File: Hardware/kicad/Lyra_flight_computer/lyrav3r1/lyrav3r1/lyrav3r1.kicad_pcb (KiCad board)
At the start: 4 copper layers, 25 x 55 mm, 89 parts, among them IC1 TESEO-LIV3F, J1 Conn_01x02, J2 Screw_Terminal_01x02, J4 Conn_01x02, J5 Conn_01x05, J7 USB_B_Micro, J8 Screw_Terminal_01x07, Q1 AO3401A, Q10 AO3400A, Q11 Q_NPN_BEC, Q2 AO3400A, Q3 AO3400A, Q4 AO3400A, Q5 AO3400A, Q7 AO3400A, Q8 AO3400A, Q9 AO3400A, U1 E22-400MM22S, U10 MT2492, U2 BMI088, U3 BMP388, U5 ADXL375BCCZ-RL7, U7 WS7916S-6/TR, U8 RP2040, U9 W25Q128JVS, X2 SX1M12.000M10F30TNN

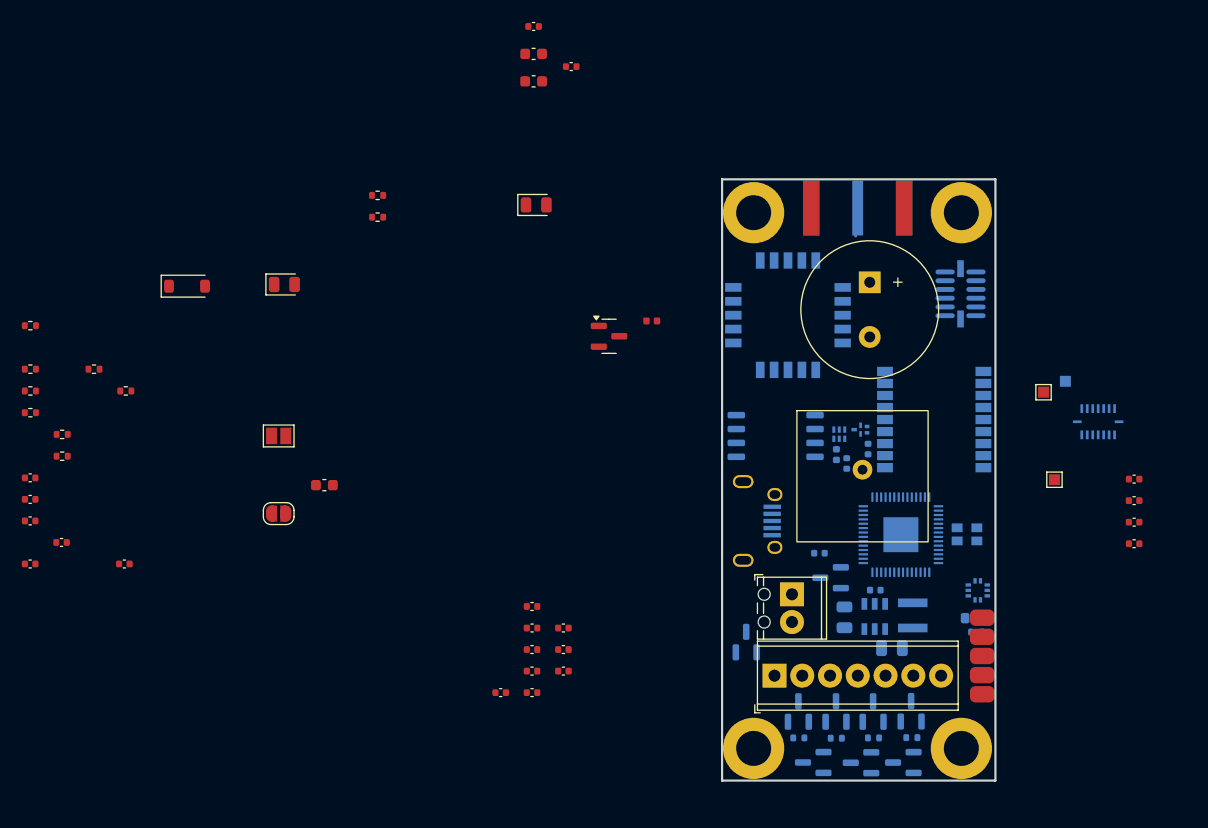
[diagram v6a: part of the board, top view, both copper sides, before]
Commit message: first pass at routing
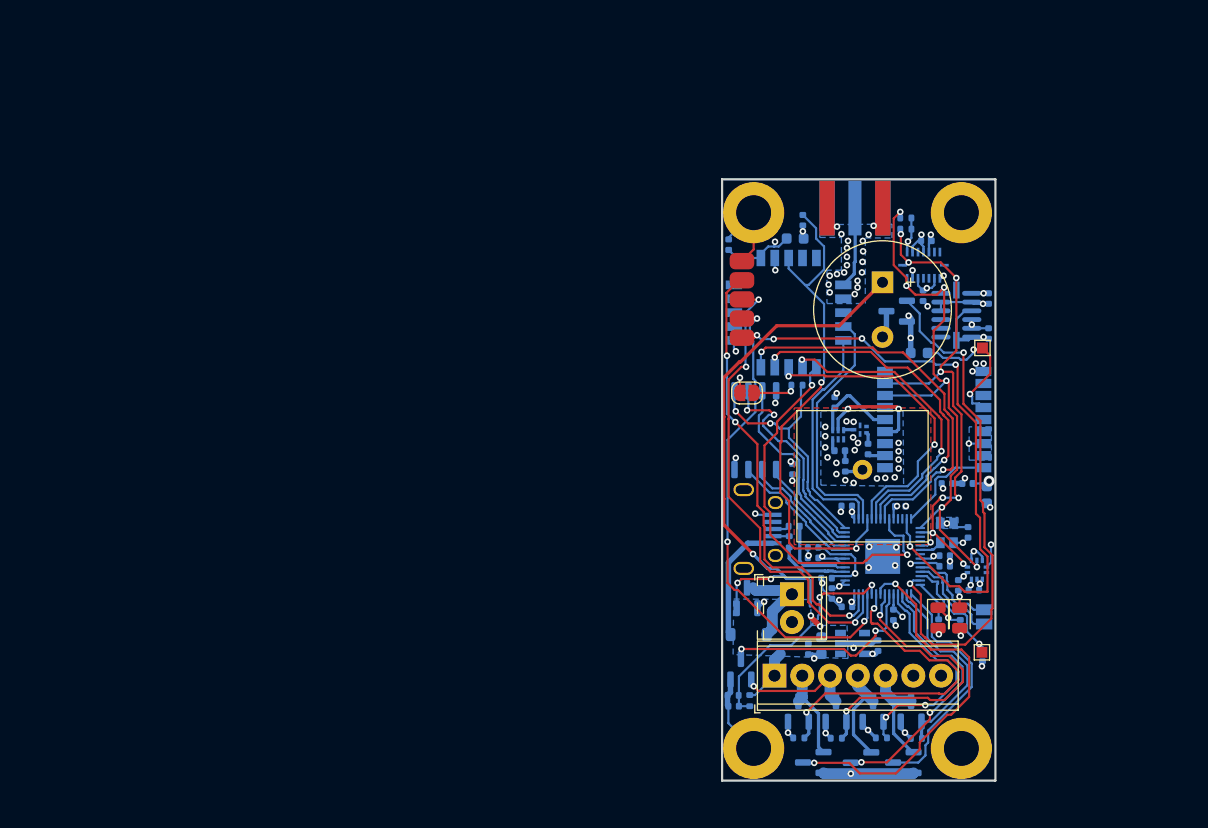
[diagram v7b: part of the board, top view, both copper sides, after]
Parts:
- removed AE2: Antenna, .pretty:SMA-SMD_HJ-SMA086
- removed C8: 1u, Capacitor_SMD:C_0402_1005Metric
- removed C9: 22u, Capacitor_SMD:C_0805_2012Metric
- removed L2: 4.7u, Inductor_SMD:L_Changjiang_FNR3015S
- removed R5: 25k, Resistor_SMD:R_0402_1005Metric
- removed R7: 110k, Resistor_SMD:R_0603_1608Metric
- removed R8: 20k, Resistor_SMD:R_0402_1005Metric
- removed TP3: TestPoint, TestPoint:TestPoint_Pad_1.0x1.0mm
- removed U10: MT2492, .pretty:SOT-23-6_L2.9-W1.6-P0.95-LS2.8-BL
- added AE3: Antenna_Shield, .pretty:CONN-SMD_KH-SMA-KE8-G, B.Cu at (195.8, 66.7)
- added C10: 10n, Capacitor_SMD:C_0402_1005Metric, B.Cu at (184.2, 70.0)
- added C11: 10u, Capacitor_SMD:C_0603_1608Metric, B.Cu at (190.3, 69.4)
- added C29: 100n, Capacitor_SMD:C_0402_1005Metric, B.Cu at (191.0, 67.8)
- added R2: 20k, Resistor_SMD:R_0402_1005Metric, B.Cu at (184.6, 111.2)
- added U6: RT9013-33GB_C19268157, .pretty:SOT-23-5_L2.9-W1.6-P0.95-LS2.8-BR, B.Cu at (195.5, 106.5)
- C1, C12, C13, C14, C16, C17, C18, C19, C2, C20, C21, C22, C24, C25, C26, C27, C28, C3, C32, C34, C4, C50, C7, D1, J1, L1, Q11, R1, R13, R14, R15, R16, R18, R28, R3, R4: moved to B.Cu
- C5: value 22u -> 1u; footprint Capacitor_SMD:C_0805_2012Metric -> Capacitor_SMD:C_0402_1005Metric
- C6: value 22nf -> 1u
- U1: value E22-400MM22S -> E22-900MM22S
- moved R1 92.2 mm to (207.4, 107.6), turned to 90 degrees
- moved R3 88.2 mm to (205.4, 104.8), turned to 90 degrees
- moved C2 85.3 mm to (202.3, 69.6), turned to 180 degrees
- moved C1 83.3 mm to (202.0, 74.7), turned to -90 degrees
- moved C13 82.9 mm to (206.1, 96.3), turned to -90 degrees
- moved R28 77.4 mm to (203.4, 104.8), turned to -90 degrees
- moved R4 71.6 mm to (186.1, 111.7), turned to -90 degrees
- moved D2 68.9 mm to (205.3, 104.1), turned to -90 degrees
- moved R14 67.4 mm to (190.4, 82.9), turned to 180 degrees
- moved R15 67.3 mm to (190.2, 95.8)
- moved J1 66.6 mm to (207.6, 104.0), turned to -90 degrees
- moved C3 66.5 mm to (184.7, 112.2), turned to 180 degrees
- moved R18 65.5 mm to (189.7, 97.2), turned to 90 degrees
- moved C27 61.7 mm to (190.0, 90.5), turned to 90 degrees
- moved D1 60.4 mm to (186.0, 105.7), turned to 180 degrees
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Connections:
- C5 pad 1: +BATT -> +3V3
- C6 pad 1: Net-(U10-BS) -> +BATT
- C6 pad 2: Net-(U10-SW) -> GND
- U1 pad 10: unconnected-(U1-RXEN-Pad10) -> /RXEN
- U1 pad 9: unconnected-(U1-TXEN-Pad9) -> /TXEN
- U8 pad 11: /DIO1 -> unconnected-(U8-GPIO8-Pad11)
- U8 pad 13: unconnected-(U8-GPIO10-Pad13) -> /BRKOUT1
- U8 pad 17: /LEDINDICATION -> unconnected-(U8-GPIO14-Pad17)
- U8 pad 18: /BRKOUT1 -> unconnected-(U8-GPIO15-Pad18)
- U8 pad 2: unconnected-(U8-GPIO0-Pad2) -> /RXEN
- U8 pad 27: unconnected-(U8-GPIO16-Pad27) -> /BUZZER
- U8 pad 28: /BUZZER -> /LEDINDICATION
- U8 pad 29: /P1 EN  -> /P1 CONT 
- U8 pad 3: /DIO3 -> /TXEN
- U8 pad 30: /P1 CONT  -> /P1 EN 
- U8 pad 31: /P2 EN  -> /P2 CONT 
- U8 pad 32: /P2 CONT  -> /P2 EN 
- U8 pad 34: /P3 EN  -> /P3 CONT 
- U8 pad 35: /P3 CONT  -> /P3 EN 
- U8 pad 36: /P4 EN  -> /P4 CONT 
- U8 pad 37: /P4 CONT  -> /P4 EN 
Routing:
- net GND: track 0.00 -> 78.2 mm, vias 0 -> 85
- net +BATT: track 0.00 -> 57.6 mm, vias 0 -> 5
- net /BRKOUT1: track 0.00 -> 54.2 mm, vias 0 -> 5
- net /SDA: track 0.00 -> 52.3 mm, vias 0 -> 6
- net +3V3: track 0.00 -> 52.0 mm, vias 0 -> 23
- net /SCL: track 0.00 -> 48.8 mm, vias 0 -> 8
- net /BUZZER: track 0.00 -> 47.5 mm, vias 0 -> 2
- net /SX RST: track 0.00 -> 47.0 mm, vias 0 -> 2
- net /BRKOUT2: track 0.00 -> 43.6 mm, vias 0 -> 3
- net /BRKOUT3: track 0.00 -> 43.2 mm, vias 0 -> 3
- net /BRKOUT4: track 0.00 -> 41.4 mm, vias 0 -> 3
- net /SCK: track 0.00 -> 36.2 mm, vias 0 -> 2
- net /BUSY: track 0.00 -> 36.0 mm, vias 0 -> 2
- net /P4 CONT : track 0.00 -> 34.7 mm, vias 0 -> 2
- net /SX CS: track 0.00 -> 33.0 mm, vias 0 -> 2
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- added copper zone on B.Cu, net +3V3
- added copper zone on B.Cu, net +BATT
- added copper zone on In1.Cu, net /BATT RAW
- added copper zone on B.Cu, net /GPS 3v3
- added copper zone on In1.Cu, net /GPS 3v3
- added copper zone on B.Cu, net GND
- added copper zone on F.Cu, net GND

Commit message: sade
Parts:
- added C8: 100n, Capacitor_SMD:C_0402_1005Metric, B.Cu at (206.7, 73.3)
- added C9: 100n, Capacitor_SMD:C_0402_1005Metric, B.Cu at (205.0, 71.0)
- added G***: LOGO, LOGO, F.Cu at (200.8, 79.5)
- added G***: LOGO, LOGO, F.Cu at (203.0, 91.2)
- added G***: LOGO, LOGO, B.Cu at (189.6, 76.1)
- added U4: LIS3MDLTR, .pretty:LGA-12_L2.0-W2.0-P0.50-BL, B.Cu at (206.9, 71.5)
- moved R4 1.59 mm to (184.6, 111.3), turned to 180 degrees
- moved R2 1.54 mm to (186.1, 111.8), turned to -90 degrees
- moved H1 0.13 mm to (186.6, 67.0)
- moved H2 0.13 mm to (205.6, 67.0)
- moved H3 0.13 mm to (186.6, 116.0)
- moved H4 0.13 mm to (205.6, 116.0)
- moved C18 0.08 mm to (193.2, 100.6)
- moved C19 0.07 mm to (193.6, 102.0)
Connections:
- R2 pad 1: /BATT SENSE  -> +BATT
- R2 pad 2: GND -> /BATT SENSE 
- R4 pad 1: +BATT -> /BATT SENSE 
- R4 pad 2: /BATT SENSE  -> GND
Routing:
- net GND: track 78.2 -> 95.9 mm, vias 85 -> 88
- net /SDA: track 52.3 -> 63.2 mm, vias 6 -> 7
- net /SCL: track 48.8 -> 53.8 mm, vias 8 -> 9
- net +3V3: track 52.0 -> 54.0 mm, vias 23 -> 25
- net Net-(U4-C1): track 0.00 -> 0.94 mm
- net /P3 EN : track 27.7 -> 28.5 mm
- net /BUZZER: track 47.5 -> 48.2 mm
- net /BRKOUT1: track 54.2 -> 54.9 mm
- net /SX RST: track 47.0 -> 47.6 mm
- net /GPS 3v3: track 2.91 -> 2.32 mm
- net /QSPI_SD1: track 19.8 -> 19.2 mm
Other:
- outline, holes or cut-outs redrawn
- board text added: "- 4 3 2 1"
- board text added: "BAT+ BAT- P1- P2- P3- P4- P+"
- board text added: "BOOT"
- board text added: "CLK"
- board text added: "JLCJLCJLCJLC"
- board text added: "LYRA V3 R1"
- board text added: "POLARIS ROCKETRY SYSTEMS"
- board text added: "PPS"
- board text added: "PWR"
- board text added: "RST"
- board text added: "SPACE IS THE PLACE"
- board text added: "STAT"
- board text added: "SW- SW+"
- board text added: "THX BB123, MATT, ELVIN, DKNIGHT, VULPES, ULYU"
- board text added: "The rocket knows where it is at all times. It knows this because it knows where it isn't."
- board text added: "U R COOL"
- board text added: "https://tinyur l.com/mt7vdux4"
- board text added: "{dblquote}<3 DAD{dblquote}"
- board text added: "{dblquote}DAWG{dblquote}"
- board text added: "{dblquote}DID YOU PLUG IT IN BACKWARDS{dblquote}"
- board text added: "{dblquote}EARTH SEEKING MISSILE{dblquote}"
- board text added: "{dblquote}IM JUST GOONIN{dblquote}"
